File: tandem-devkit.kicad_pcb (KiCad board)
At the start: 2 copper layers, 95.4 x 100 mm, 87 parts, among them J101 Conn_01x02, J301 FPC24(0.5MM), J302 FPC10(0.5MM), Q301 2N7002, Q302 2N7002, Q303 AO3401A, U201 AMS1117-ADJ_SOT223

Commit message: Pre routing: footprints&parts
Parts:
- removed the REF** at (190.3, 56.7)
- removed the REF** at (143.7, 56.9)
- added J102: QWIIC I2C Connector, project-lib:JST_SHL_SM04B-SHLS-TF_1x04-1MP_P1.00mm_Horizontal, F.Cu at (181.6, 20.3)
- added R110: 22, Resistor_SMD:R_0603_1608Metric, F.Cu at (188.0, 20.8)
- added R111: 22, Resistor_SMD:R_0603_1608Metric, F.Cu at (188.0, 18.2)
- D201: footprint Diode_SMD:D_SMB -> Package_TO_SOT_SMD:SOT-23
- D204, D307, D308, D309: value MDD SS14 -> B5819W; footprint Diode_SMD:D_SMA -> Diode_SMD:D_SOD-123
- D205, D206: value SM4007PL -> B5819W
- locked: footprint project-lib:TouchSlider-3_30x8mm-covered -> project-lib:TouchSlider-3_30x13mm-covered
- moved D309 15.1 mm to (157.5, 61.0)
- moved D201 1.47 mm to (133.3, 38.1), turned to -90 degrees
- renumbered R110 to R112, R111 to R113
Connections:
- A101 pad 17: unconnected-(A101-Pad17) -> Net-(A101-Pad17)
- A101 pad 18: unconnected-(A101-Pad18) -> Net-(A101-Pad18)
- A102 pad 17: unconnected-(A101-Pad17) -> Net-(A101-Pad17)
- A102 pad 18: unconnected-(A101-Pad18) -> Net-(A101-Pad18)

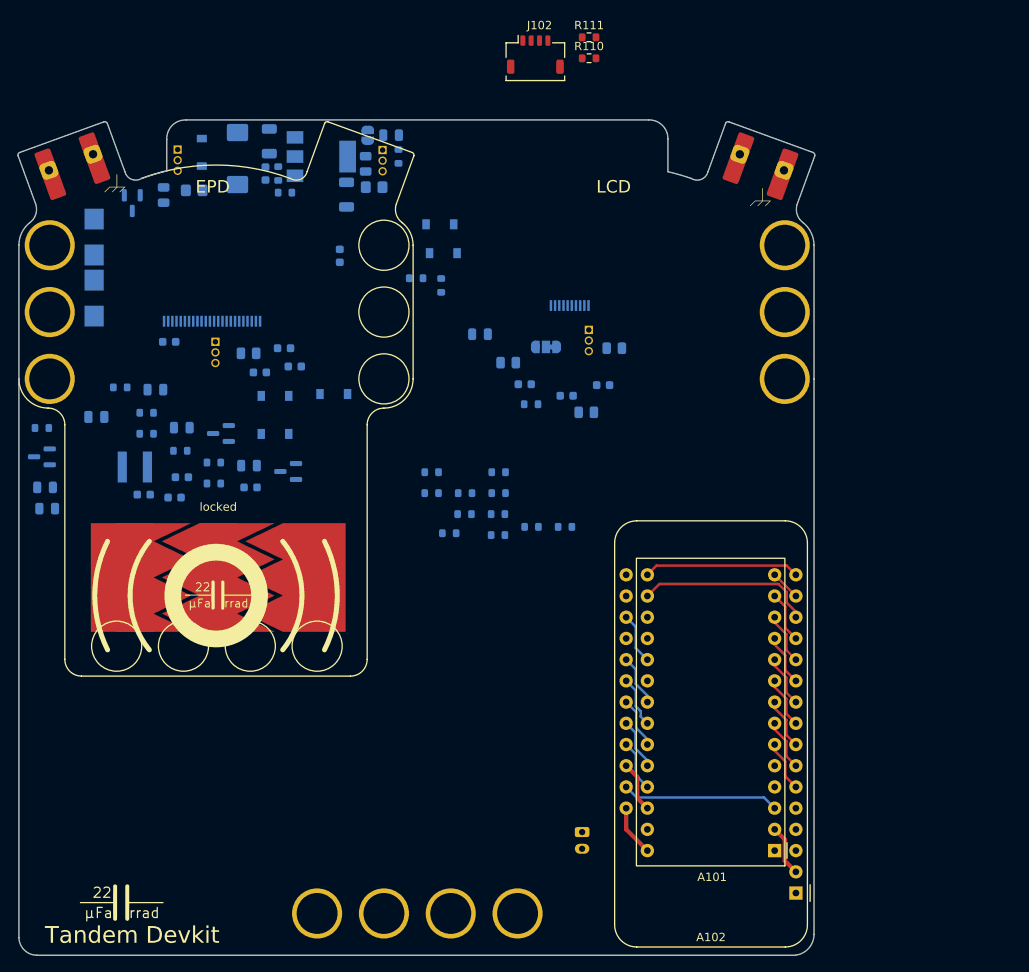
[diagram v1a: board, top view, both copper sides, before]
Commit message: PCB: include schematic changes
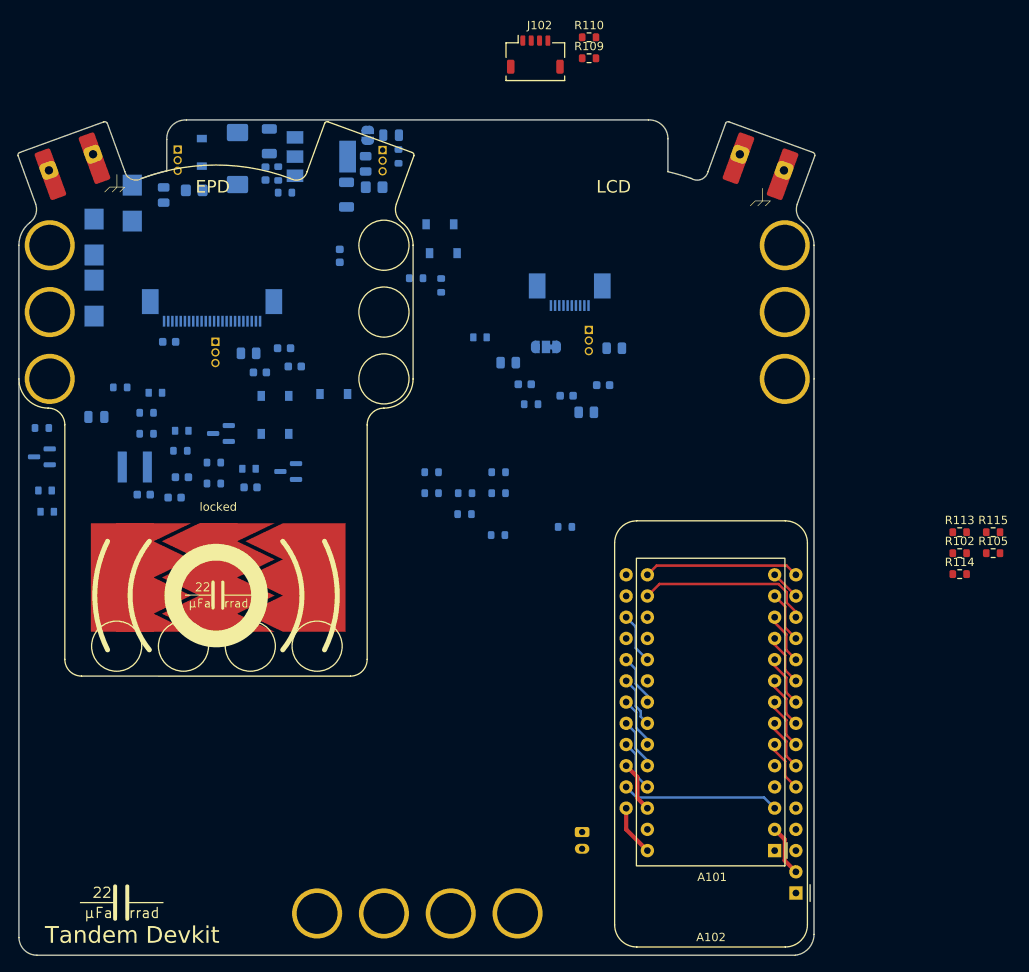
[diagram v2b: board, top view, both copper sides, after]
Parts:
- removed the R104 at (181.1, 76.9)
- removed the R108 at (171.3, 77.6)
- removed the R109 at (177.1, 75.3)
- added R102: 22, Resistor_SMD:R_0603_1608Metric, F.Cu at (232.4, 80.0)
- added R105: 22, Resistor_SMD:R_0603_1608Metric, F.Cu at (236.4, 80.0)
- added R113: 22, Resistor_SMD:R_0603_1608Metric, F.Cu at (232.4, 77.5)
- added R114: 15k, Resistor_SMD:R_0603_1608Metric, F.Cu at (232.4, 82.5)
- added R115: 15k, Resistor_SMD:R_0603_1608Metric, F.Cu at (236.4, 77.5)
- D201: value SMBJ170CA -> TVS Diode; footprint Package_TO_SOT_SMD:SOT-23 -> Diode_SMD:D_SMB
- D301, D302, D303, D304, D305, D306: footprint LED_SMD:LED_0805_2012Metric -> project-lib:LED_sidemount
- renumbered R102 to R103, R103 to R104, R105 to R106, R106 to R107, R107 to R108, R110 to R109, R111 to R110, R112 to R111, R113 to R112
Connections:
- A101 pad 1: unconnected-(A101-Pad1) -> Net-(A101-Pad1)
- A101 pad 20: unconnected-(A101-Pad20) -> Net-(A101-Pad20)
- A101 pad 5: unconnected-(A101-Pad5) -> /CAP_TOUCH_1
- A101 pad 6: /CAP_TOUCH_1 -> /EPD_CURRENT_SENSE
- A101 pad 7: /EPD_CURRENT_SENSE -> /LCD_CURRENT_SENSE
- A101 pad 8: /LCD_CURRENT_SENSE -> Net-(A101-Pad8)
- A102 pad 1: unconnected-(A101-Pad1) -> Net-(A101-Pad1)
- A102 pad 20: unconnected-(A101-Pad20) -> Net-(A101-Pad20)
- A102 pad 5: unconnected-(A101-Pad5) -> /CAP_TOUCH_1
- A102 pad 6: /CAP_TOUCH_1 -> /EPD_CURRENT_SENSE
- A102 pad 7: /EPD_CURRENT_SENSE -> /LCD_CURRENT_SENSE
- A102 pad 8: /LCD_CURRENT_SENSE -> Net-(A101-Pad8)
- J102 pad MP: (no net) -> GND
- R111 pad 2: Net-(A101-Pad9) -> Net-(A101-Pad8)
- R112 pad 2: Net-(A101-Pad10) -> Net-(A101-Pad9)
- R304 pad 2: /EPD_CURRENT_SENSE -> /LCD_CURRENT_SENSE
- R306 pad 2: /EPD_CURRENT_SENSE -> /LCD_CURRENT_SENSE
- R308 pad 2: /EPD_CURRENT_SENSE -> /LCD_CURRENT_SENSE
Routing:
- net /CAP_TOUCH_1: track 6.13 -> 0.00 mm
- net Net-(A101-Pad8): track 0.00 -> 6.13 mm

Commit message: PCB: rough placement, 1/x
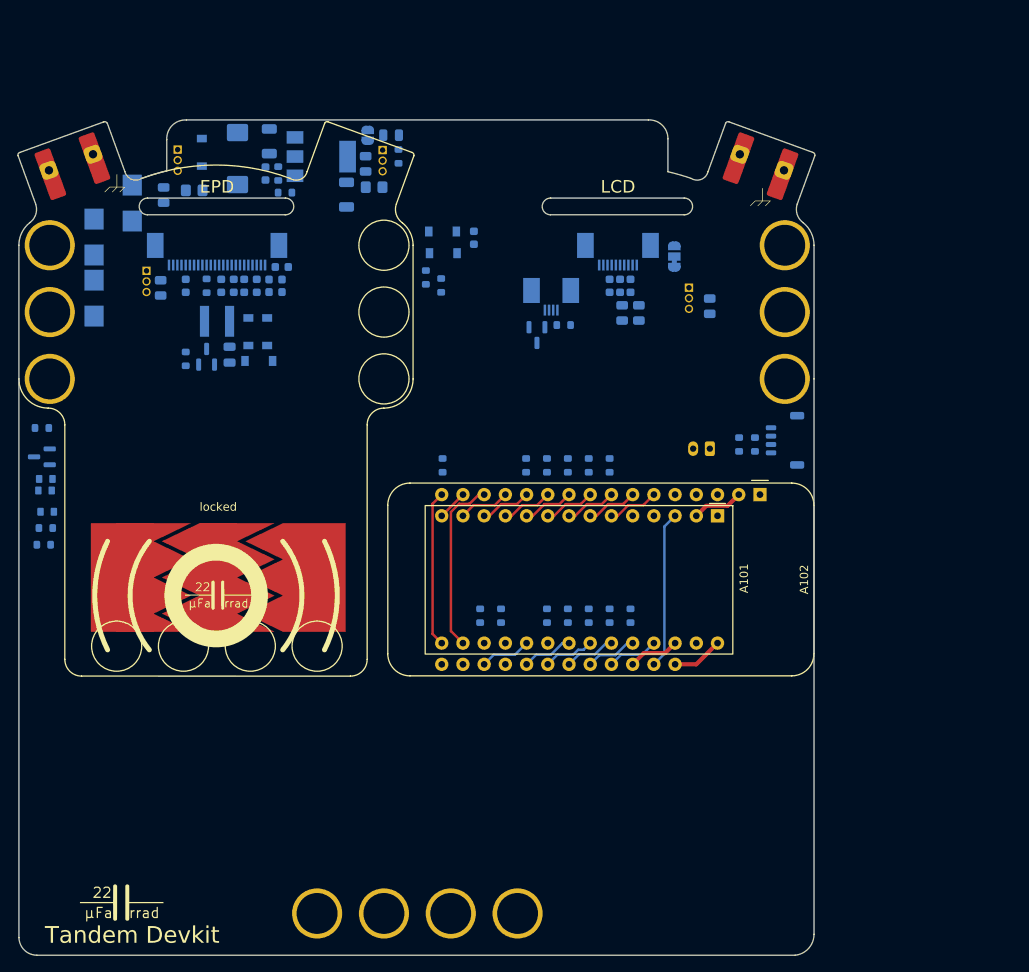
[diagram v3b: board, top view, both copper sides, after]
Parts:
- removed the D302 at (175.0, 53.8)
- removed the D304 at (147.3, 69.5)
- removed the D306 at (139.3, 65.0)
- removed the R304 at (181.1, 62.2)
- removed the R308 at (135.1, 65.7)
- added DISP301: Display_generic, project-lib:154_Epaper_Display, F.Cu at (143.5, 57.1)
- added DISP302: Display_generic, project-lib:154_Epaper_Display, F.Cu at (191.5, 57.1)
- added J301: ConnectorLCDFrontLight, project-lib:jlcpcb-C11047_FFC_1x04-1MP_P0.50mm_Horizontal, B.Cu at (183.5, 50.9)
- J102, R102, R105, R109, R110, R113, R114, R115: moved to B.Cu
- moved R110 70.0 mm to (177.5, 87.5), turned to -90 degrees
- moved R109 68.0 mm to (175.0, 87.5), turned to -90 degrees
- moved J102 55.0 mm to (211.5, 66.5), turned to -90 degrees
- moved R304 53.6 mm to (185.0, 52.7), turned to 0 degrees
- moved R102 50.0 mm to (183.0, 87.5), turned to -90 degrees
- moved J101 48.4 mm to (202.5, 67.5), turned to 180 degrees
- moved A102 47.9 mm to (208.5, 73.0), turned to -90 degrees
- moved R113 47.6 mm to (185.5, 69.5), turned to -90 degrees
- moved R105 46.5 mm to (190.5, 87.5), turned to -90 degrees
- moved A101 40.7 mm to (203.4, 75.5), turned to -90 degrees
- moved Q302 34.0 mm to (181.8, 53.9), turned to -90 degrees
- moved R115 32.2 mm to (206.0, 67.0), turned to 90 degrees
- moved R114 29.0 mm to (207.9, 67.0), turned to 90 degrees
- moved R106 28.0 mm to (193.0, 87.5), turned to -90 degrees
- moved C304 27.2 mm to (145.5, 48.0), turned to 90 degrees
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- renumbered D303 to D302, D305 to D303, D307 to D304, D308 to D305, D309 to D306, J301 to J302, J302 to J303, R306 to R304, R307 to R306, R309 to R307, R310 to R308
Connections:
- C303 pad 2: GND -> /EPD_CURRENT_SENSE
- C311 pad 2: GND -> /EPD_CURRENT_SENSE
- JP301 pad 3: GND -> /LCD_CURRENT_SENSE

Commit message: PCB: rough placement, 2/x
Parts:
- D201: value TVS Diode -> P6SMB6.8CA
- D202, D203: value SMBJ5342 -> LBZT52C7V5T1G; footprint Diode_SMD:D_SMB -> Diode_SMD:D_SOD-123
- moved R102 21.9 mm to (183.3, 65.6)
- moved R103 21.9 mm to (185.8, 65.6)
- moved R104 21.9 mm to (188.3, 65.6)
- moved R105 21.9 mm to (190.8, 65.6)
- moved R106 21.9 mm to (193.3, 65.6)
- moved R109 21.9 mm to (175.3, 65.6)
- moved R110 21.9 mm to (177.8, 65.6)
- moved D203 6.82 mm to (132.7, 43.9)
- moved R301 5.30 mm to (139.3, 52.9)
- moved TP301 5.30 mm to (137.6, 50.9)
- moved D202 4.92 mm to (132.7, 39.2)
- moved D201 4.71 mm to (129.3, 40.5), turned to 90 degrees

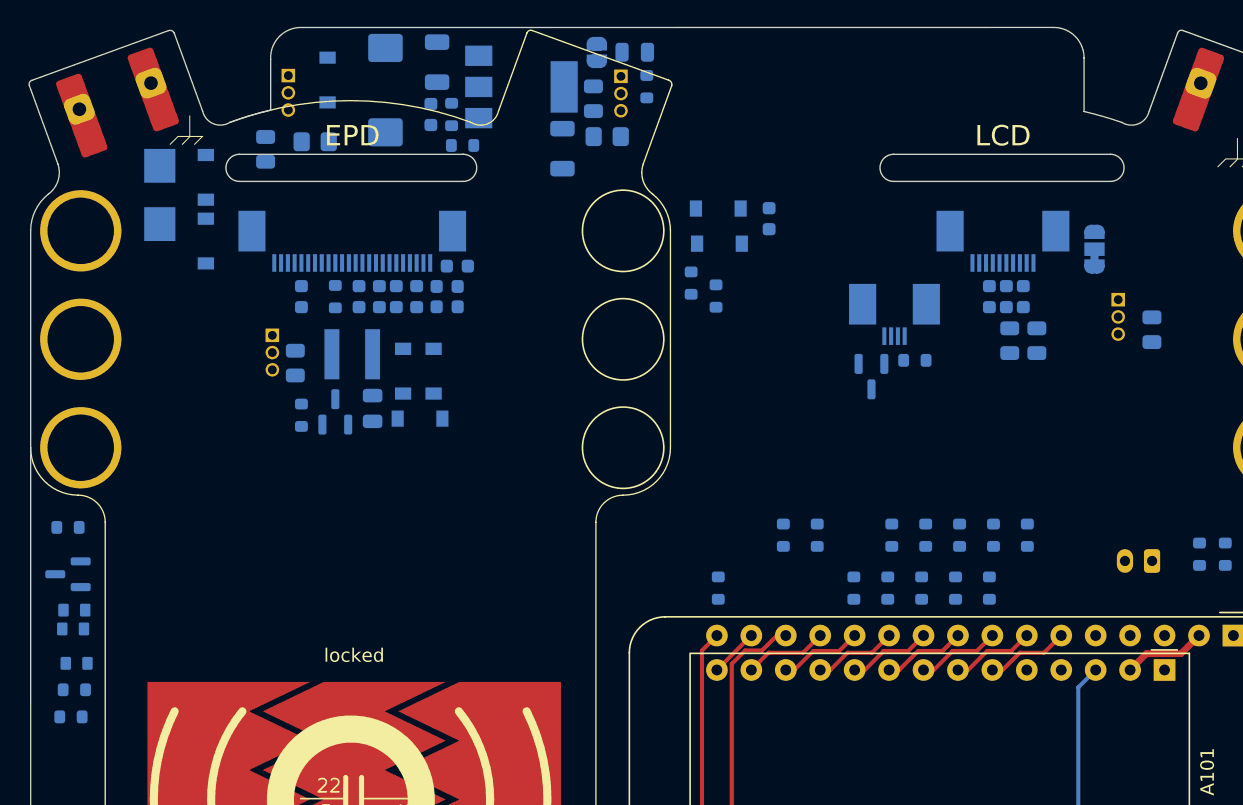
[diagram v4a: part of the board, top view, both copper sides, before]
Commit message: PCB: rough placement, 3/x
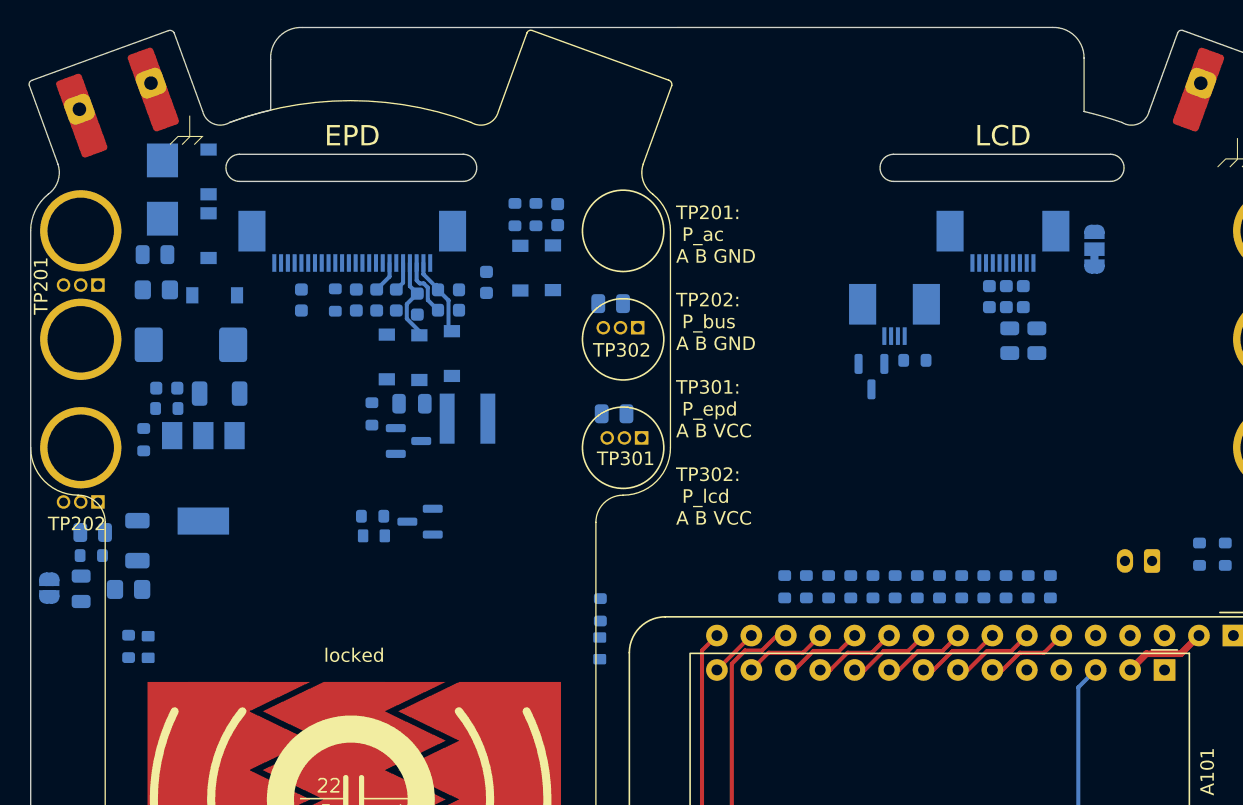
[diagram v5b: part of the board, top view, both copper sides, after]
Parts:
- TP201, TP202, TP301, TP302: footprint Connector_PinHeader_1.27mm:PinHeader_1x03_P1.27mm_Vertical -> project-lib:TestPoint_1x03_P1.27mm
- moved D207 56.9 mm to (123.5, 69.5), turned to -90 degrees
- moved JP201 56.5 mm to (121.2, 69.5), turned to -90 degrees
- moved R208 53.6 mm to (124.2, 67.1), turned to 0 degrees
- moved TP202 49.7 mm to (124.7, 63.1), turned to 90 degrees
- moved R207 48.9 mm to (124.3, 65.4), turned to 180 degrees
- moved R209 48.6 mm to (127.0, 69.6)
- moved C205 42.7 mm to (127.7, 66.0)
- moved R302 40.0 mm to (162.6, 48.5), turned to 0 degrees
- moved R306 39.2 mm to (161.8, 71.1), turned to 90 degrees
- moved D303 38.5 mm to (161.4, 73.9), turned to -90 degrees
- moved U201 37.2 mm to (132.5, 61.4), turned to -90 degrees
- moved TP302 35.5 mm to (164.6, 50.3), turned to 90 degrees
- moved R206 32.0 mm to (128.1, 58.6), turned to -90 degrees
- moved R205 30.2 mm to (129.8, 56.3), turned to 180 degrees
- moved C203 29.2 mm to (133.7, 55.2), turned to 180 degrees
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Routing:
- net /Display/PREVGL: track 0.00 -> 5.96 mm
- net /Display/PREVGH: track 0.00 -> 5.67 mm
- net Net-(C308-Pad2): track 0.00 -> 4.30 mm
- net Net-(C304-Pad2): track 0.00 -> 2.35 mm
- net Net-(C305-Pad2): track 0.00 -> 2.16 mm
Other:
- board text added: "Experiment with display and side-mount LEDs in this area"
- board text added: "Remove R206 and R209 when using external power supply board."
- board text added: "TP201: P_ac A B GND TP202: P_bus A B GND TP301: P_epd A B VCC TP302: P_lcd A B VCC"

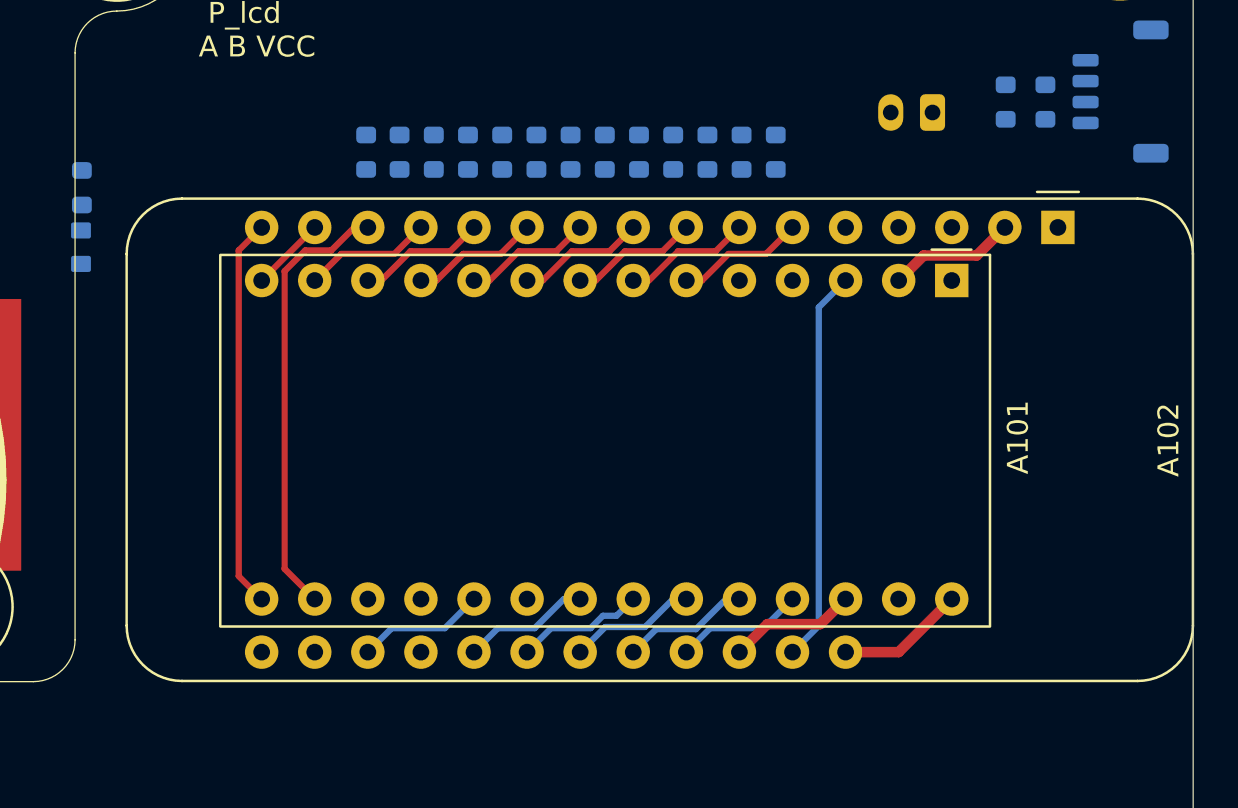
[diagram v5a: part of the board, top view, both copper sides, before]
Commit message: PCB: flip feather so it can be soldered directly underneath the board
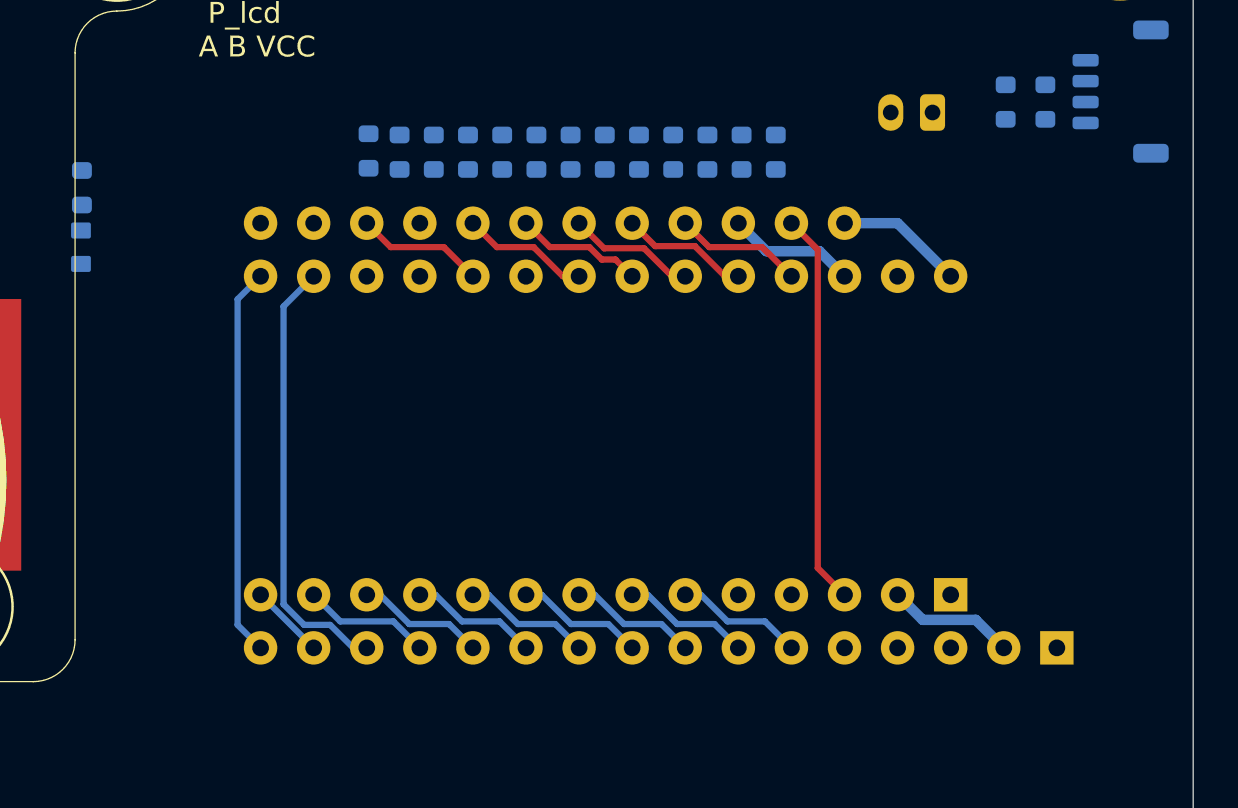
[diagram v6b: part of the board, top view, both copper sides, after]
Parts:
- A101, A102: moved to B.Cu
- moved A102 20.1 mm to (208.4, 93.1), turned to 90 degrees
- moved A101 15.0 mm to (203.4, 90.6), turned to 90 degrees
- moved R101 0.13 mm to (175.5, 69.3)
